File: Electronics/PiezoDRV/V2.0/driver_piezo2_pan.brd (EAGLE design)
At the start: 36 x 70 mm, 37 parts, among them J1 RJ12STRAIGHT-ANALOG, T1 FMMT718

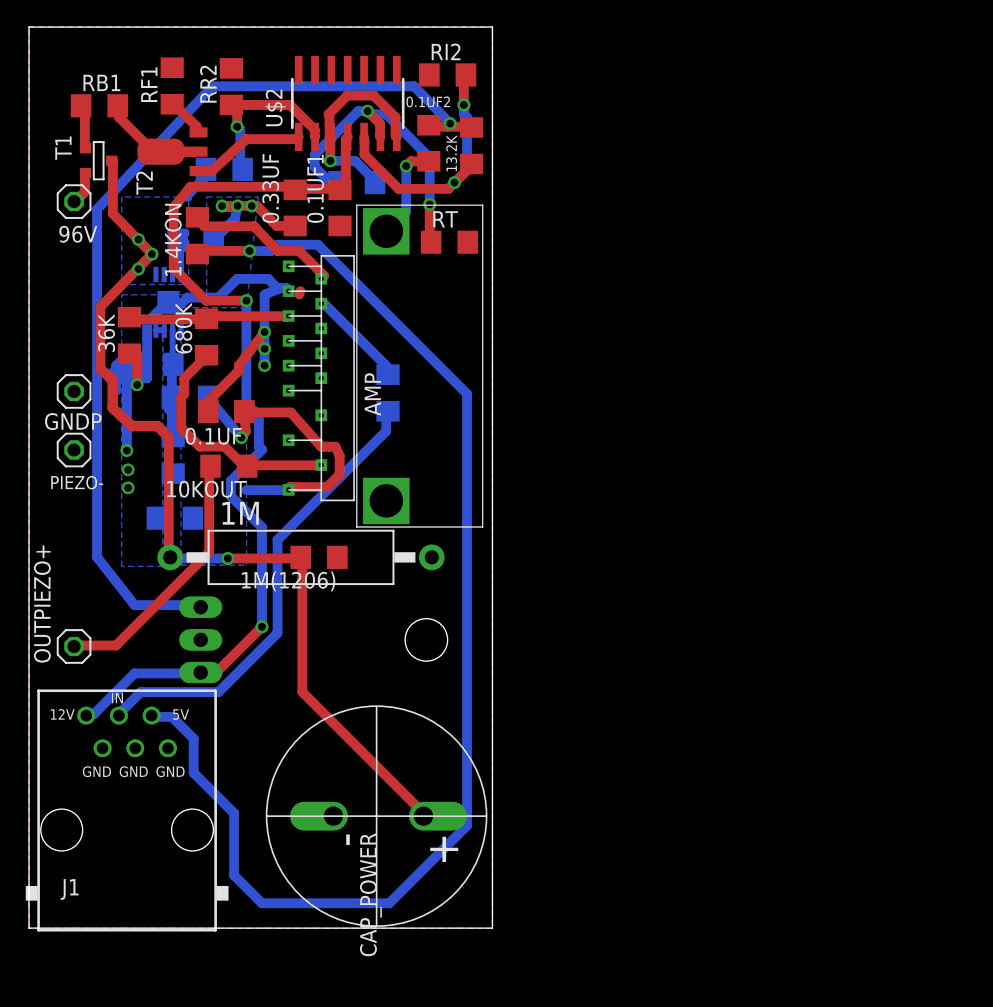
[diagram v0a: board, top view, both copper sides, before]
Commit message: corrections on piezo driver v2.0, generated gerbers
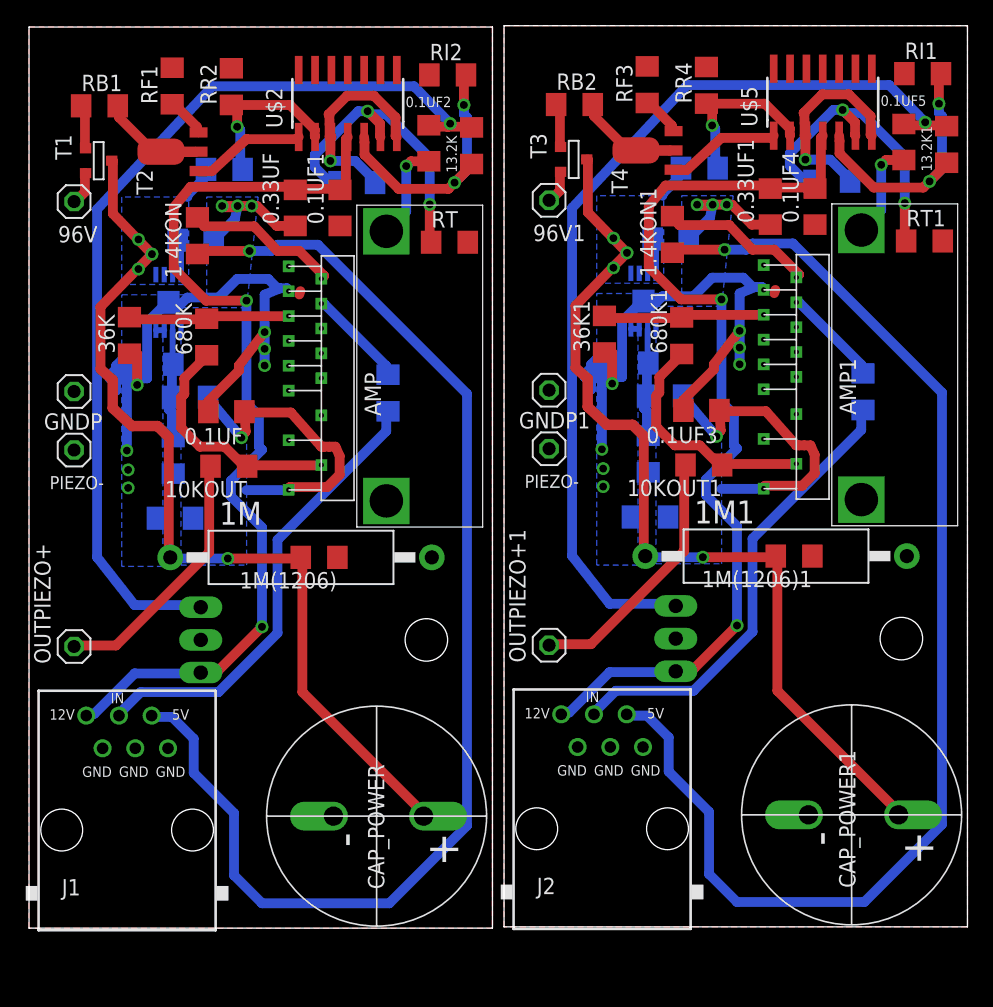
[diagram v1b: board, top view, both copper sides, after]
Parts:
- added 0.1UF3, 0.1UF4, 0.1UF5, 0.33UF1, CBYP10NF1, CIN10UF1, COUT10UF1: (no value), rcl:C1206
- added 1.32K1, 1.4KON1, 100K1, 10KIN1, 10KOUT1, 1M(1206)1, 36K1, 680K1: (no value), resistor:R1206
- added 13.2K1: 13.2K, resistor:R1206
- added 1M1: (no value), resistor-power:CA0002
- added 96V1, GND1, GNDP1, OUTPIEZO+1: (no value), pinhead:1X01
- added AMP1: POWER_AMP_LME49811TB, PIEZO_LBR:POWER_AMP_LME49811TB
- added CAP_POWER1: CAP200VCAP200V, PIEZO_LBR:CAP200V
- added J2: RJ12STRAIGHT-ANALOG, lpatiny:RJ12-STRAIGHT-ANALOG
- added LD001: TPS7A4001, PIEZO_LBR:S-PDSO-G08
- added RB2: 100k, resistor:R1206
- added RF2, RF3, RT1: 10k, resistor:R1206
- added RI1: 280k, resistor:R1206
- added RR3: 810k-806k, resistor:R1206
- added RR4: 90k, resistor:R1206
- added T3: FMMT718, zetex:SOT-23
- added T4: (no value), zetex:SOT89
- added U$4: DISIPADOR, PIEZO_LBR:DISIPADOR
- added U$5: LM324, PIEZO_LBR:SO14
- added U$6: 7805, PIEZO_LBR:TO220
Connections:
- new net 12V1: 0.1UF4.2, 0.33UF1.2, J2.+12V, U$5.4, U$6.1
- new net 1OUT1: T4.1, U$5.1
- new net 2IN+1: 13.2K1.1, RI1.2, U$5.5
- new net 2IN-1: RF2.1, RT1.1, U$5.6
- new net 2OUT1: RF2.2, U$5.3, U$5.7
- new net 5V1: 1.4KON1.1, J2.+5V
- new net 5VOP1: 0.1UF5.2, 13.2K1.2, U$6.3
- new net B1: 36K1.2, 680K1.2, AMP1.IN-
- new net FB1: 1.32K1.2, 100K1.1, CBYP10NF1.2, LD001.2
- new net GND1: 0.1UF3.2, 0.1UF4.1, 0.1UF5.1, 0.33UF1.1, 1.32K1.1, 1M(1206)1.1, 1M1.2, 36K1.1, AMP1.-VEE, AMP1.GND, CAP_POWER1.-, CIN10UF1.1, COUT10UF1.2, GND1.1, GNDP1.1, J2.GND1, J2.GND2, J2.GND3, LD001.3, LD001.4, LD001.TH, RF3.2, RI1.1, RR4.2, RT1.2, U$4.P$1, U$4.P$2, U$5.11, U$6.2
- new net IN_AMP1: 10KIN1.2, AMP1.IN+
- new net IN_VOLTAGE1: 10KIN1.1, J2.IN
- new net N$1: RB2.2, T4.2, T4.2@1
- new net N$2: RB2.1, T3.3
- new net N$6: RF3.1, T4.3
- new net ON1: 1.4KON1.2, AMP1.SD
- new net OUT_PIEZO1: 10KOUT1.2, OUTPIEZO+1.1
- new net SOURCE1: 10KOUT1.1, 680K1.1, AMP1.SOURCE
- new net V1: 0.1UF3.1, 100K1.2, AMP1.VCC, CBYP10NF1.1, COUT10UF1.1, LD001.1
- new net VF1: RR3.2, RR4.1, U$5.2
- new net VIN1: 1M(1206)1.2, 1M1.1, CAP_POWER1.+, CIN10UF1.2, LD001.5, LD001.8, RR3.1, T3.1
- new net VINS1: 96V1.1, T3.2
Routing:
- net 5V1: track 0.00 -> 97.0 mm, vias 0 -> 1
- net VIN1: track 0.00 -> 77.0 mm, vias 0 -> 4
- net 12V1: track 0.00 -> 74.1 mm, vias 0 -> 2
- net 5VOP1: track 0.00 -> 73.4 mm, vias 0 -> 1
- net GND1: track 0.00 -> 72.8 mm, vias 0 -> 11
- net IN_VOLTAGE1: track 0.00 -> 35.8 mm
- net V1: track 0.00 -> 24.5 mm, vias 0 -> 1
- net 2IN-1: track 0.00 -> 24.2 mm, vias 0 -> 2
- net 2IN+1: track 0.00 -> 20.6 mm, vias 0 -> 2
- net OUT_PIEZO1: track 0.00 -> 20.2 mm
- net SOURCE1: track 0.00 -> 18.6 mm
- net 2OUT1: track 0.00 -> 16.1 mm, vias 0 -> 1
- net VF1: track 0.00 -> 13.3 mm, vias 0 -> 1
- net B1: track 0.00 -> 12.5 mm
- net ON1: track 0.00 -> 12.1 mm
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- added copper zone on layer 1, net GND1
- added copper zone on layer 16, net GND1
- added copper zone on layer 16, net V1
- added copper zone on layer 16, net VIN1
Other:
- board size 36 x 70 mm -> 72.9 x 70.1 mm
